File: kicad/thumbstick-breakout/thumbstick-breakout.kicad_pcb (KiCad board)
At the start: 2 copper layers, 25.4 x 31.8 mm, 9 parts, among them J1 59453-051110ECHLF

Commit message: extend breakout
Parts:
- moved J1 5.76 mm to (150.0, 121.2)
- moved JP1 4.76 mm to (150.0, 116.5)
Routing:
- net /HORZ: track 2.78 -> 11.4 mm
- net GND: track 45.5 -> 51.8 mm
- net VCC: track 26.9 -> 32.5 mm
- net /SEL: track 23.3 -> 28.6 mm
- net /VERT: track 21.6 -> 25.2 mm
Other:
- board size 25.4 x 31.8 mm -> 25.4 x 37.7 mm

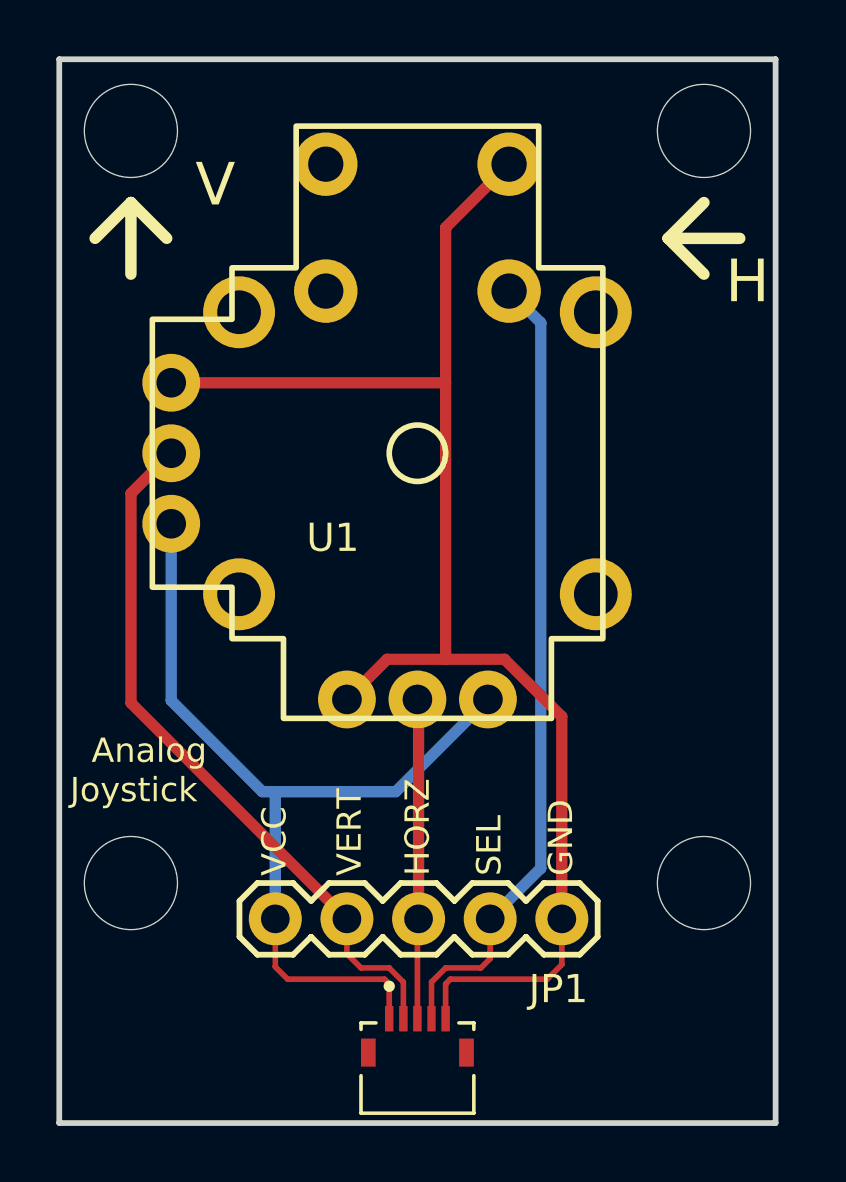
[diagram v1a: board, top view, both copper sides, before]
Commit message: Use only fcc on thumbstick
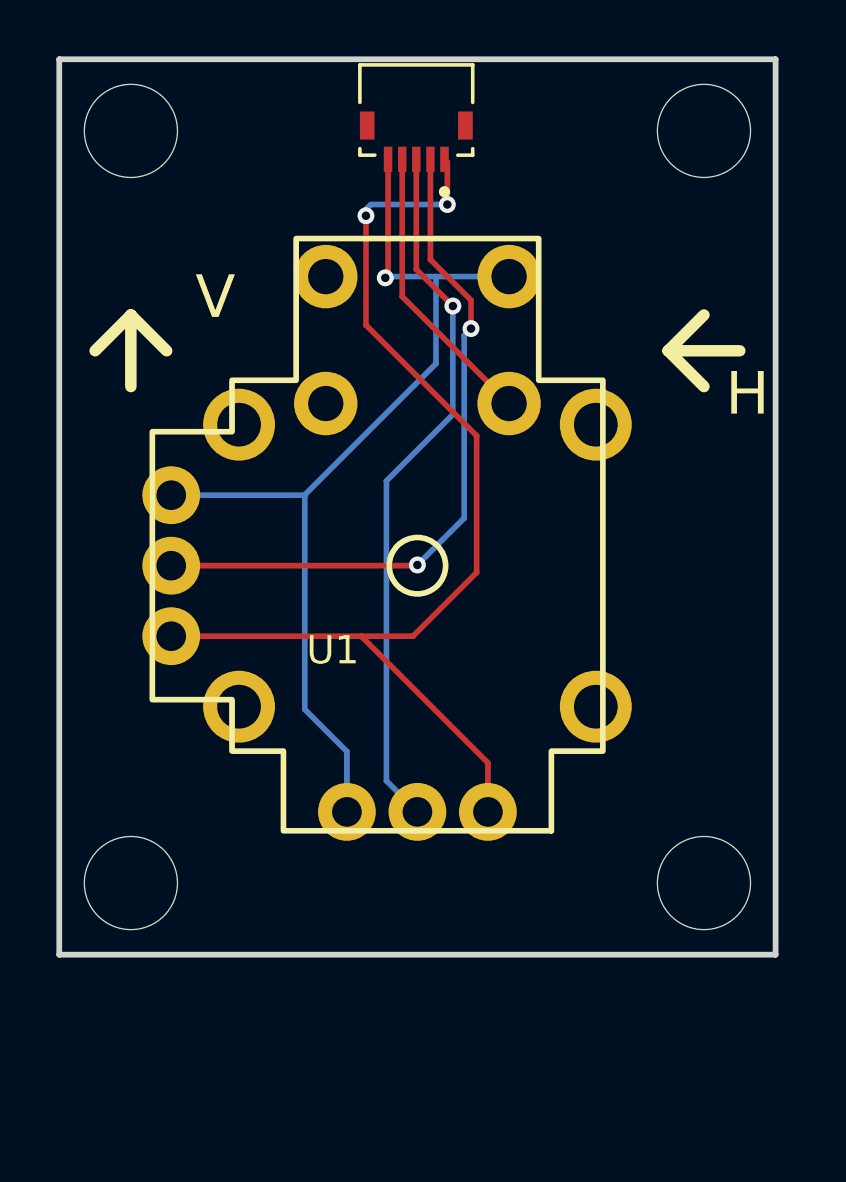
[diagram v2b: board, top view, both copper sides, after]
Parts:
- removed G***: LOGO, LOGO
- removed JP1: ~, thumbstick-breakout:1x05
- removed REF**: OSHW-Symbol_6.7x6mm_SilkScreen, Symbol:OSHW-Symbol_6.7x6mm_SilkScreen
- moved J1 32.9 mm to (150.0, 88.4), turned to 180 degrees
- moved U1 3.99 mm to (150.0, 104.0)
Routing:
- net /SEL: track 28.6 -> 10.2 mm
- net GND: track 51.8 -> 34.9 mm, vias 0 -> 1
- net /HORZ: track 11.4 -> 25.1 mm, vias 0 -> 1
- net VCC: track 32.5 -> 39.0 mm, vias 0 -> 2
- net /VERT: track 25.2 -> 24.5 mm, vias 0 -> 2
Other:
- board size 25.4 x 37.7 mm -> 25.4 x 31.8 mm
- board text removed: "${REVISION}"
- board text removed: "Analog"
- board text removed: "Designed by: Daniel Benoy CC BY SA 4.0 danielbenoy.com"
- board text removed: "GND"
- board text removed: "HORZ"
- board text removed: "Joystick"
- board text removed: "SEL"
- board text removed: "VCC"
- board text removed: "VERT"
- board text removed: "dbenoy"
